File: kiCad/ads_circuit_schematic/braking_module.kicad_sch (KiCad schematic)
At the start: 0 parts

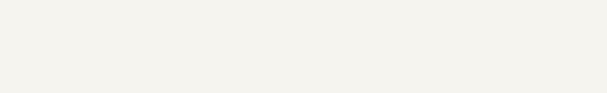
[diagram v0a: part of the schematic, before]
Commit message: Added new symbols for linear actuators, added fuses, added 5V step down
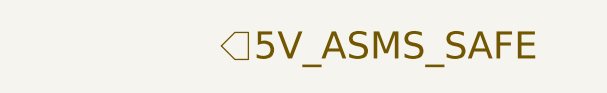
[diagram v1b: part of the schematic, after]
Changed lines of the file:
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@@
+		)
+	)
+	(hierarchical_label "5V_ASMS_SAFE"
+		(shape input)
+		(at 139.7 31.75 0)
+		(effects
+			(font
+				(size 3 3)
+				(color 255 0 0 1)
+			)
+			(justify left)
 		)
 	)

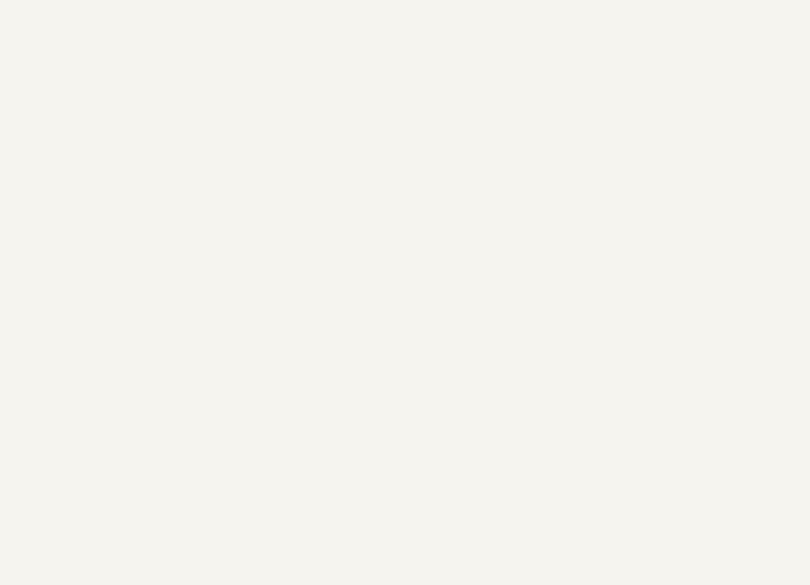
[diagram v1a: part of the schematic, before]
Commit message: added breaking motor
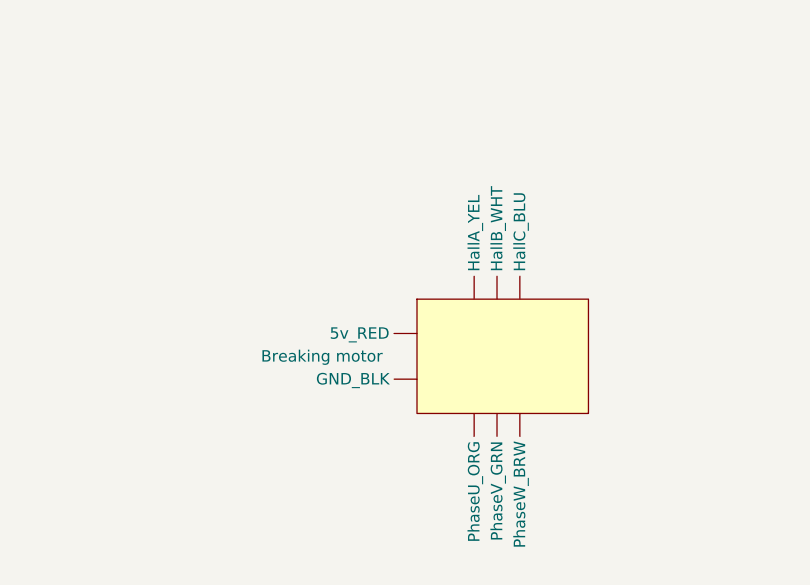
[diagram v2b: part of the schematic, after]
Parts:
- added U1: Breaking motor, symbol steering_motor:breaking_motor
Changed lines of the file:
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@@
+		)
+	)
+	(symbol
+		(lib_id "steering_motor:breaking_motor")
+		(at 140.97 99.06 0)
+		(unit 1)
+		(exclude_from_sim no)
+		(in_bom yes)
+		(on_board yes)
+		(dnp no)
+		(fields_autoplaced yes)
+		(property "Reference" "U1"
+			(at 140.97 99.06 0)
+			(effects
+				(font
+					(size 1.27 1.27)
+				)
+				(hide yes)
+			)
+		)
+		(property "Value" "Breaking motor"
+			(at 118.11 92.7099 0)
+			(effects
+				(font
+					(size 1.27 1.27)
+				)
+				(justify right)
+			)
+		)
+		(property "Footprint" ""
+			(at 140.97 99.06 0)
+			(effects
+				(font
+					(size 1.27 1.27)
+				)
+				(hide yes)
+			)
+		)
+		(property "Datasheet" ""
+			(at 140.97 99.06 0)
+			(effects
+				(font
+					(size 1.27 1.27)
+				)
+				(hide yes)
+			)
+		)
+		(property "Description" ""
+			(at 140.97 99.06 0)
+			(effects
+				(font
+					(size 1.27 1.27)
+				)
+				(hide yes)
+			)
+		)
+		(pin ""
+		)
+		(pin ""
+		)
+		(pin ""
+		)
+		(pin ""
+		)
+		(pin ""
+		)
+		(pin ""
+		)
+		(pin ""
+		)
+		(pin ""
+		)
+		(instances
+			(project ""
+				(path "/71fa6abf-14fe-4383-b55d-b9c0203d051b/5cc4a821-9cfe-4f60-9e3a-3af94c154a2b"
+					(reference "U1")
+					(unit 1)
+				)
+			)
 		)
 	)
